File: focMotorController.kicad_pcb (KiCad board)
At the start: 4 copper layers, 95.5 x 61 mm, 55 parts, among them J2 JST-PH encoder connection, P1 WJ128V-5.0-3P, P2 Power input, U1 74LVC2T45DC, U10 IR2104 Gate Driver B, U11 IR2104 Gate Driver C, U12 Amplifier A, U13 Amplifier B, U14 Amplifier C, U2 74LVC2T45DC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

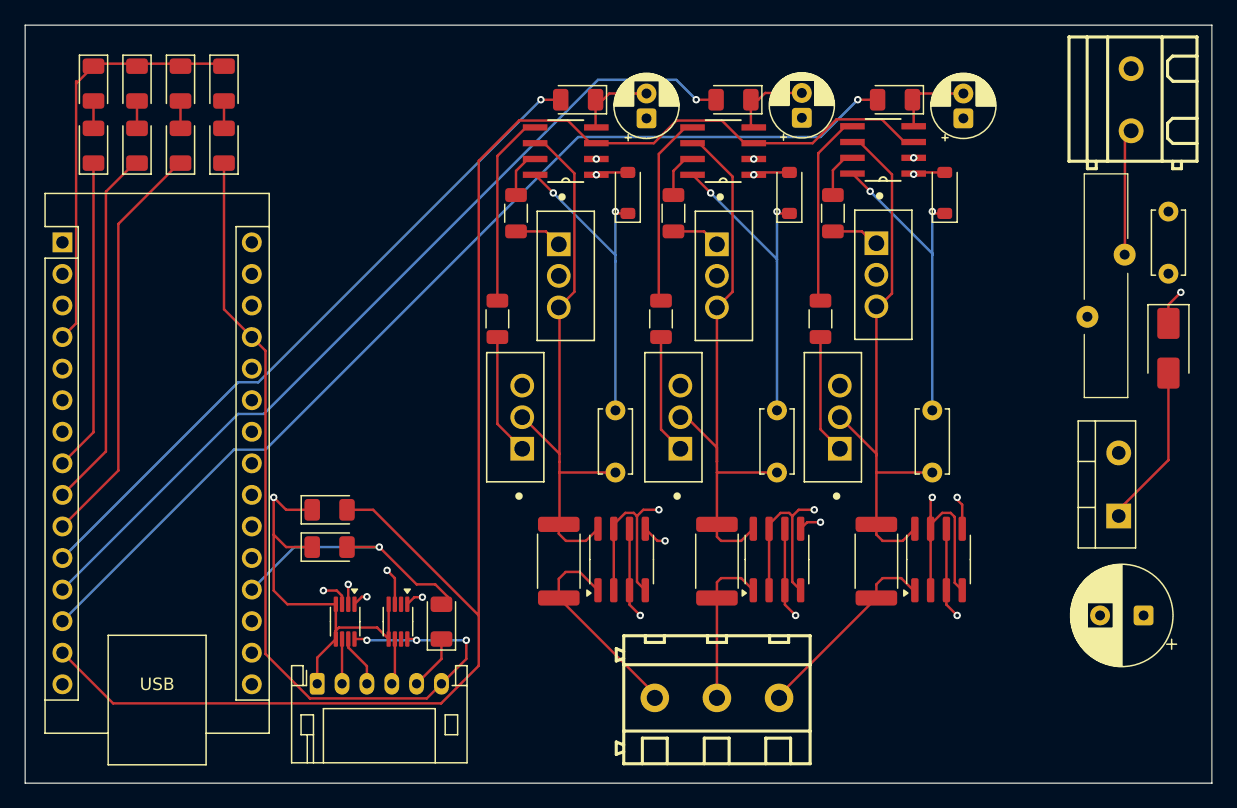
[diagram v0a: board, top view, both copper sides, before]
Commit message: Compact PCB
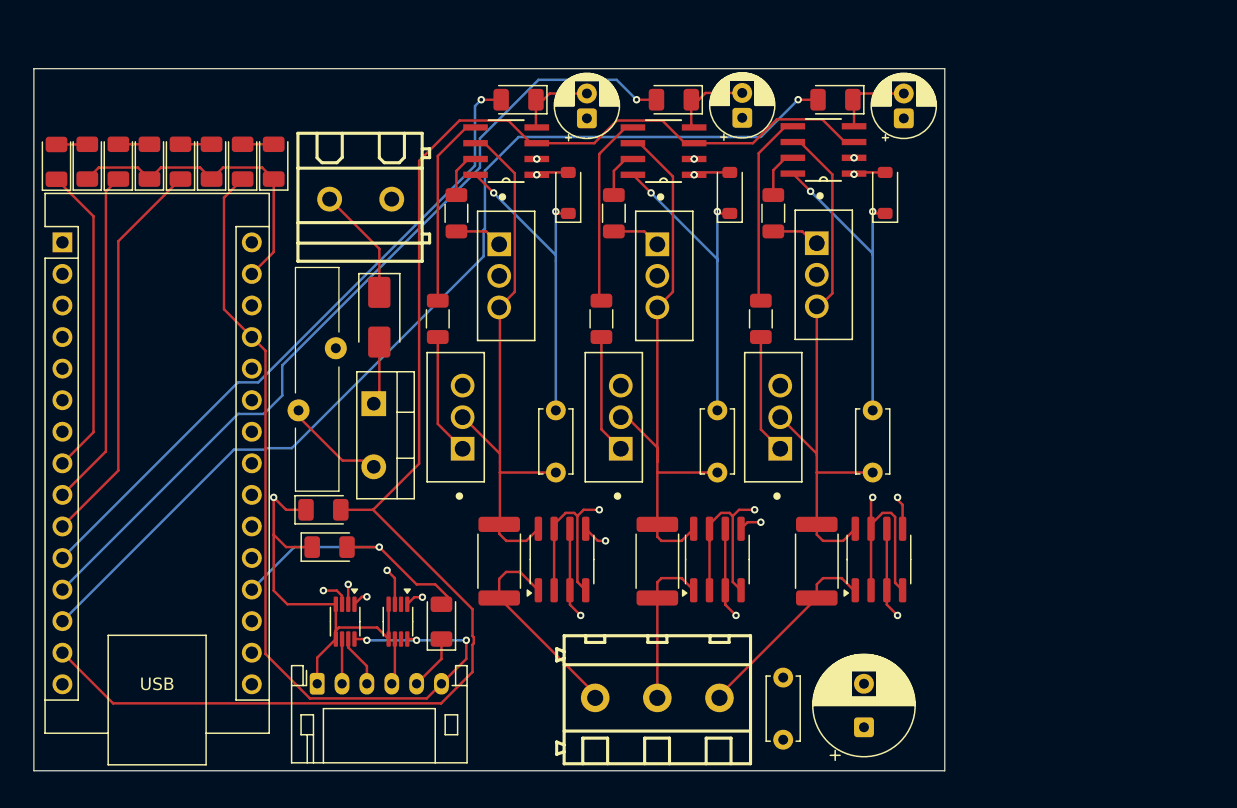
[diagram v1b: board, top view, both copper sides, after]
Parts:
- moved F1 63.9 mm to (95.8, 58.0)
- moved D1 63.5 mm to (101.0, 53.0)
- moved P2 62.5 mm to (99.5, 43.5), turned to 180 degrees
- moved D2 60.6 mm to (100.5, 60.0), turned to -90 degrees
- moved C2 48.7 mm to (133.5, 82.0)
- moved C1 24.2 mm to (140.0, 86.0), turned to 90 degrees
- moved D3 7.45 mm to (92.5, 40.5), turned to 90 degrees
- moved D6 6.76 mm to (87.5, 40.5), turned to 90 degrees
- moved D5 6.36 mm to (82.5, 40.5), turned to 90 degrees
- moved D4 6.30 mm to (77.5, 40.5), turned to 90 degrees
- moved U11 4.80 mm to (136.7, 39.5)
- moved C3 4.80 mm to (115.2, 60.5)
- moved C8 4.80 mm to (117.7, 37.0)
- moved D7 4.80 mm to (116.2, 43.0)
- moved P1 4.80 mm to (123.4, 83.6)
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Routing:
- net Net-(C1-Pad1): track 28.3 -> 6.91 mm
- net PVIN: track 168.0 -> 155.7 mm
- net GND: track 354.5 -> 344.8 mm, vias 5 -> 4
- net 3.3VDD: track 103.9 -> 96.5 mm
- net Enable: track 131.4 -> 124.1 mm
- net CurrentA: track 35.8 -> 31.0 mm
- net CurrentC: track 59.9 -> 55.1 mm
- net CurrentB: track 47.7 -> 42.9 mm
- net Net-(D2-A): track 11.7 -> 7.52 mm
- net +12V: track 10.2 -> 14.4 mm
- net Status2: track 29.4 -> 27.3 mm
- net PhaseA: track 62.0 -> 60.0 mm
- net PhaseB: track 76.9 -> 75.0 mm
- net Status3: track 33.4 -> 32.0 mm
- net 5VDD: track 71.4 -> 70.5 mm
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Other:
- board size 95.5 x 61 mm -> 73.3 x 56.5 mm

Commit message: Finish initial PCB version
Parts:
- moved C8 7.06 mm to (116.5, 44.0)
- moved C6 7.04 mm to (129.5, 44.0)
- moved C7 6.99 mm to (142.5, 44.0)
- moved D9 5.56 mm to (142.5, 48.5)
- moved D7 5.51 mm to (116.5, 48.5)
- moved D8 5.51 mm to (129.5, 48.5)
- moved R7 4.57 mm to (110.0, 39.5)
- moved R8 4.35 mm to (123.0, 39.5)
- moved R12 4.26 mm to (134.5, 48.5)
- moved R9 4.19 mm to (121.5, 48.5)
- moved R11 4.18 mm to (136.5, 39.5)
- moved R22 4.08 mm to (108.5, 48.5)
- moved U9 4.05 mm to (110.0, 43.5)
- moved U11 4.03 mm to (136.0, 43.5)
- moved U10 3.96 mm to (123.0, 43.5)
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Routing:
- net PVIN: track 155.7 -> 107.2 mm, vias 3 -> 0
- net GND: track 344.8 -> 315.6 mm, vias 4 -> 5
- net Enable: track 124.1 -> 136.5 mm
- net CurrentC: track 55.1 -> 67.5 mm
- net BLowGate: track 9.64 -> 19.7 mm
- net Net-(U11-LO): track 14.8 -> 23.8 mm
- net Net-(U10-LO): track 14.9 -> 23.1 mm
- net Net-(D2-A): track 7.52 -> 0.00 mm
- net Net-(U9-LO): track 14.9 -> 22.4 mm
- net PhaseC: track 88.8 -> 94.0 mm, vias 2 -> 1
- net PhaseA: track 60.0 -> 55.2 mm, vias 2 -> 1
- net CurrentB: track 42.9 -> 47.1 mm
- net Net-(D8-K): track 27.2 -> 24.2 mm
- net Net-(D7-K): track 26.7 -> 23.9 mm
- net CLowGate: track 9.64 -> 12.1 mm
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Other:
- board size 73.3 x 56.5 mm -> 72.8 x 52.5 mm

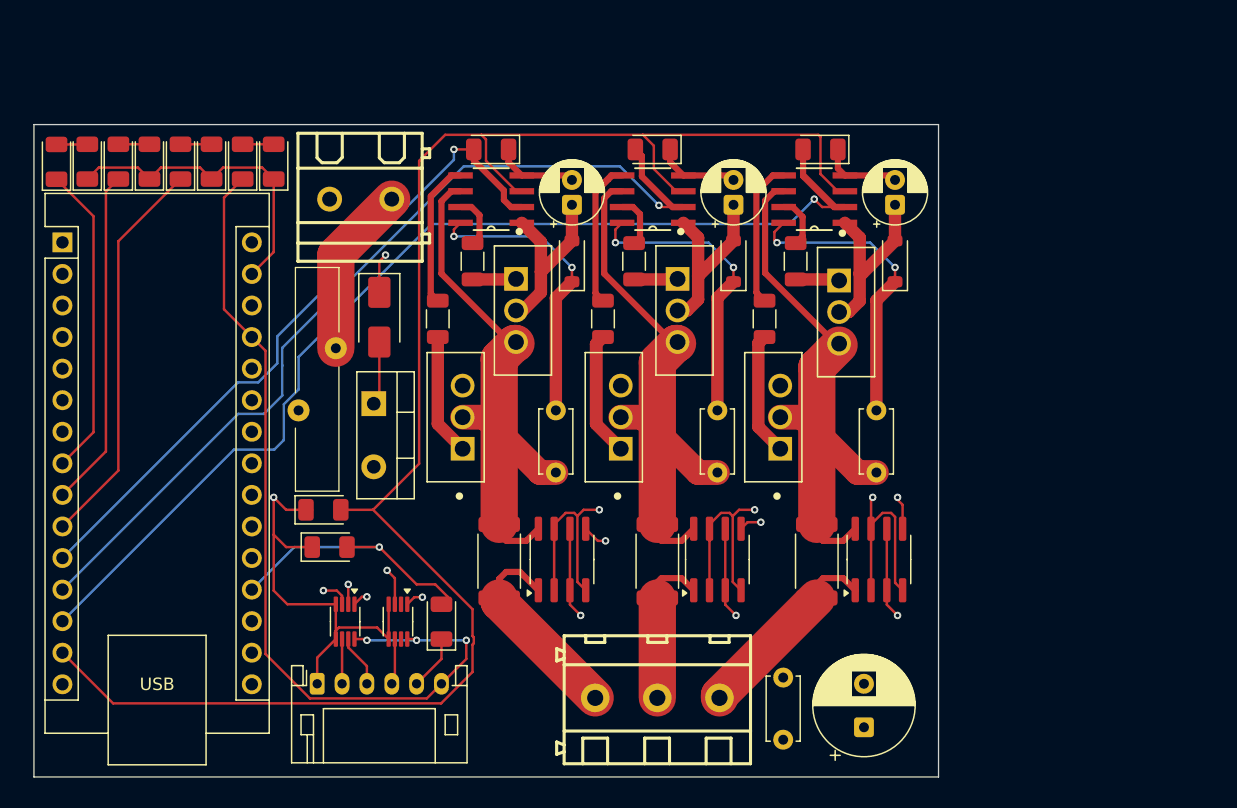
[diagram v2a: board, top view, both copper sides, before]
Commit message: Update schematics with remaining JLCPCB parts, finish BOM, and export manufacturing files
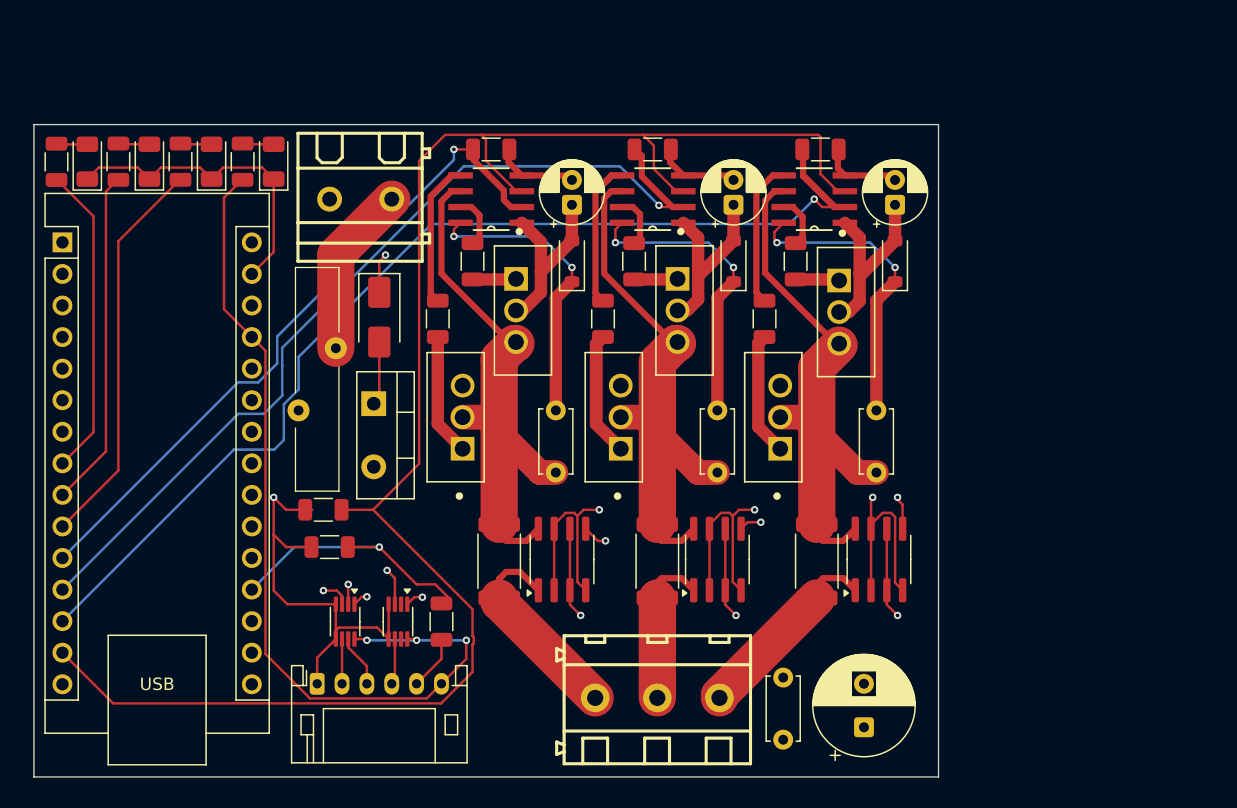
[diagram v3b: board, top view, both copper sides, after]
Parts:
- R1, R11, R13, R2, R3, R4, R5, R6, R7, R8: footprint LED_SMD:LED_1206_3216Metric -> Resistor_SMD:R_1206_3216Metric

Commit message: Add copper pours for high current traces and clean up PCB elsewhere
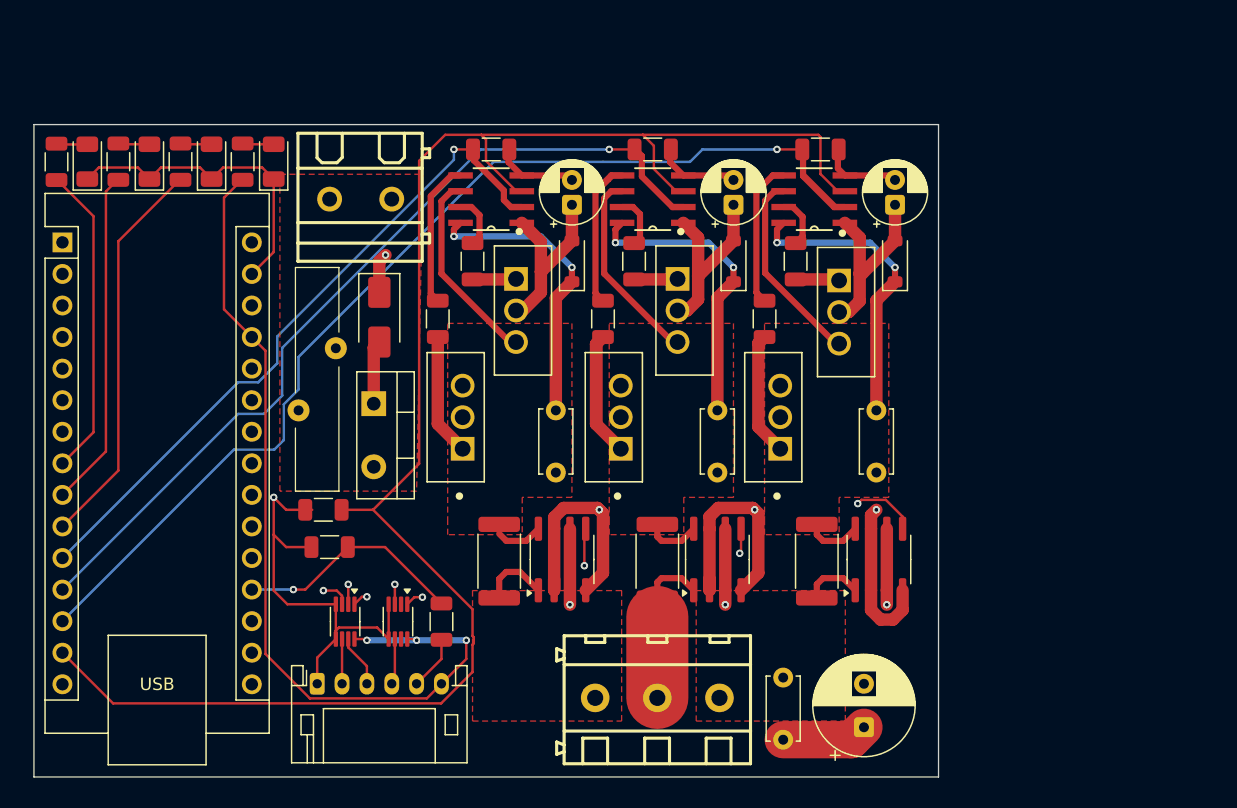
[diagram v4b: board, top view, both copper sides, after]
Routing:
- net GND: track 315.6 -> 137.9 mm
- net PVIN: track 107.2 -> 56.8 mm
- net PhaseBSense: track 46.0 -> 21.1 mm
- net PhaseASense: track 45.1 -> 20.5 mm
- net PhaseCSense: track 44.4 -> 20.5 mm
- net +12V: track 13.9 -> 0.00 mm
- net PhaseCOut: track 16.3 -> 4.80 mm
- net PhaseAOut: track 18.0 -> 6.74 mm
- net 3.3VDD: track 96.5 -> 106.8 mm
- net CurrentC: track 67.5 -> 57.1 mm
- net CurrentB: track 47.1 -> 42.2 mm
- net PhaseB: track 74.4 -> 69.7 mm
- net Net-(A1-A0): track 21.5 -> 18.6 mm
- net PhaseC: track 94.0 -> 91.9 mm
- net PhaseBOut: track 12.8 -> 11.2 mm
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- added copper zone on F.Cu, net +12V
- added copper zone on In1.Cu, net GND
- added copper zone on In2.Cu, net PVIN
- added copper zone on F.Cu, net PhaseAOut
- added copper zone on F.Cu, net PhaseASense
- added copper zone on F.Cu, net PhaseBSense
- added copper zone on F.Cu, net PhaseCOut
- added copper zone on F.Cu, net PhaseCSense
